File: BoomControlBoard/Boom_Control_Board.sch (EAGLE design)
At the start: 31 parts, among them IC1 L298, J1 Servo Header, J2 FTDI Header, U1 ATMEGA328P_TQFP, Y1 16MHz

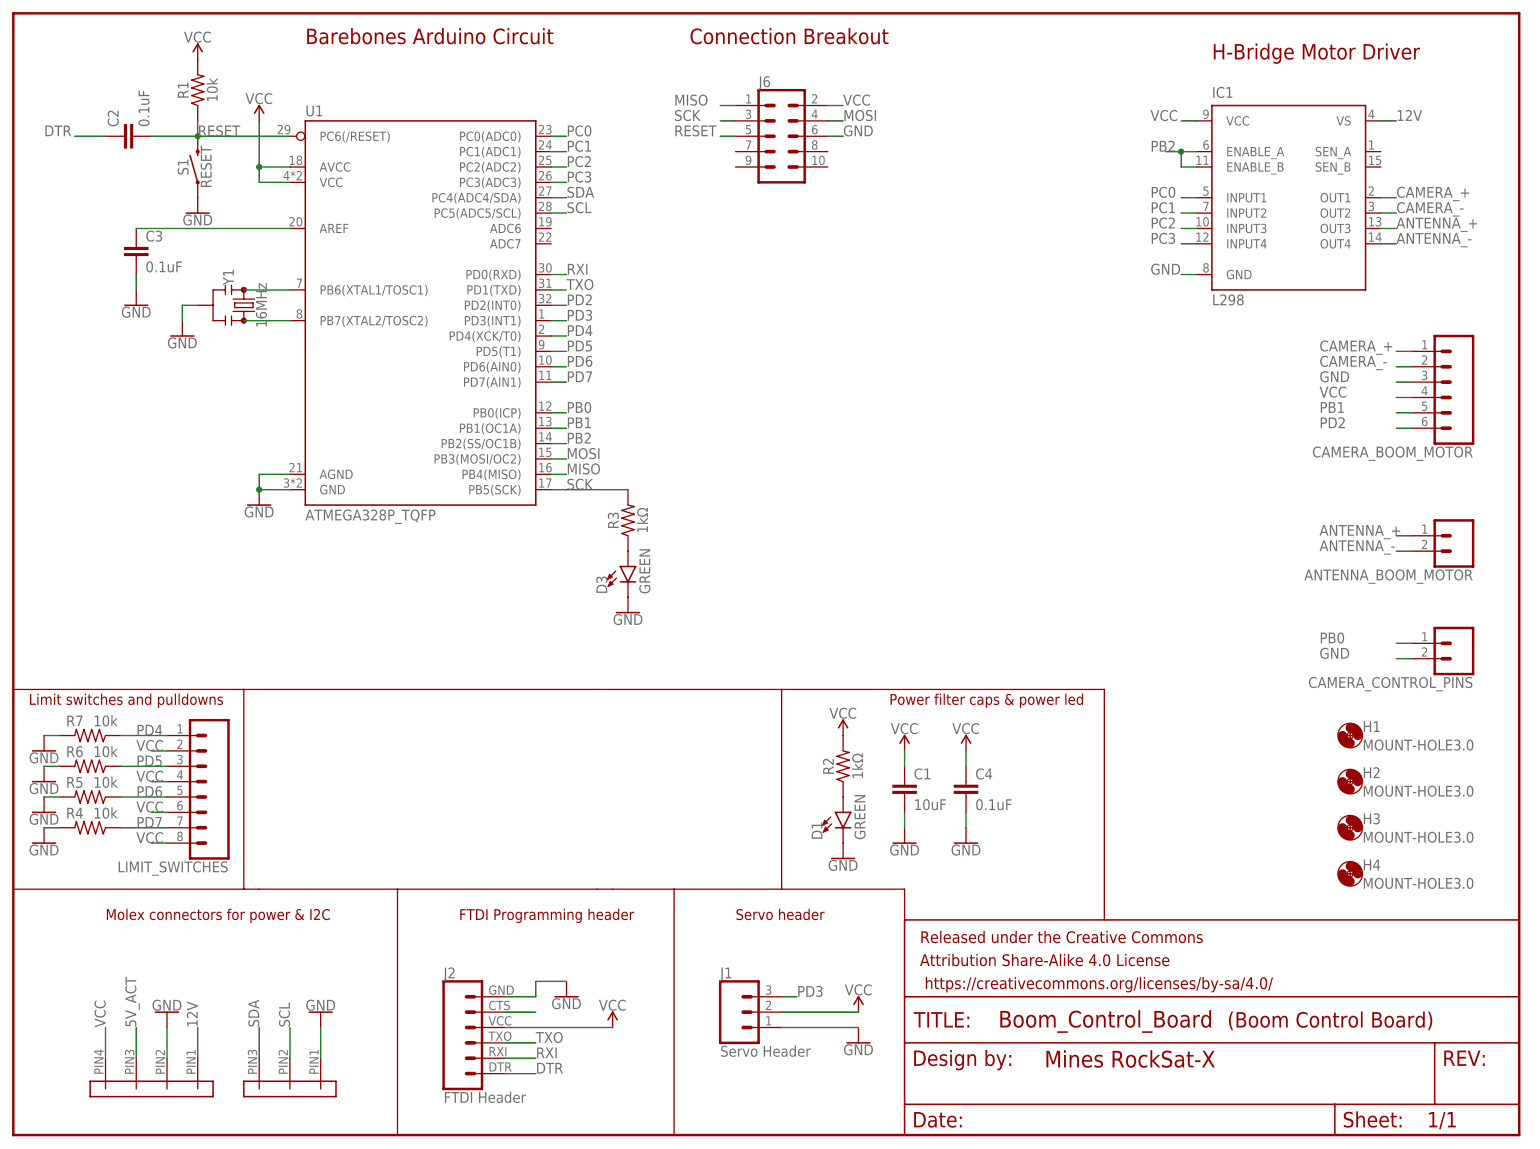
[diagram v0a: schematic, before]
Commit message: minor aesthetic adjustments to boom control board schem
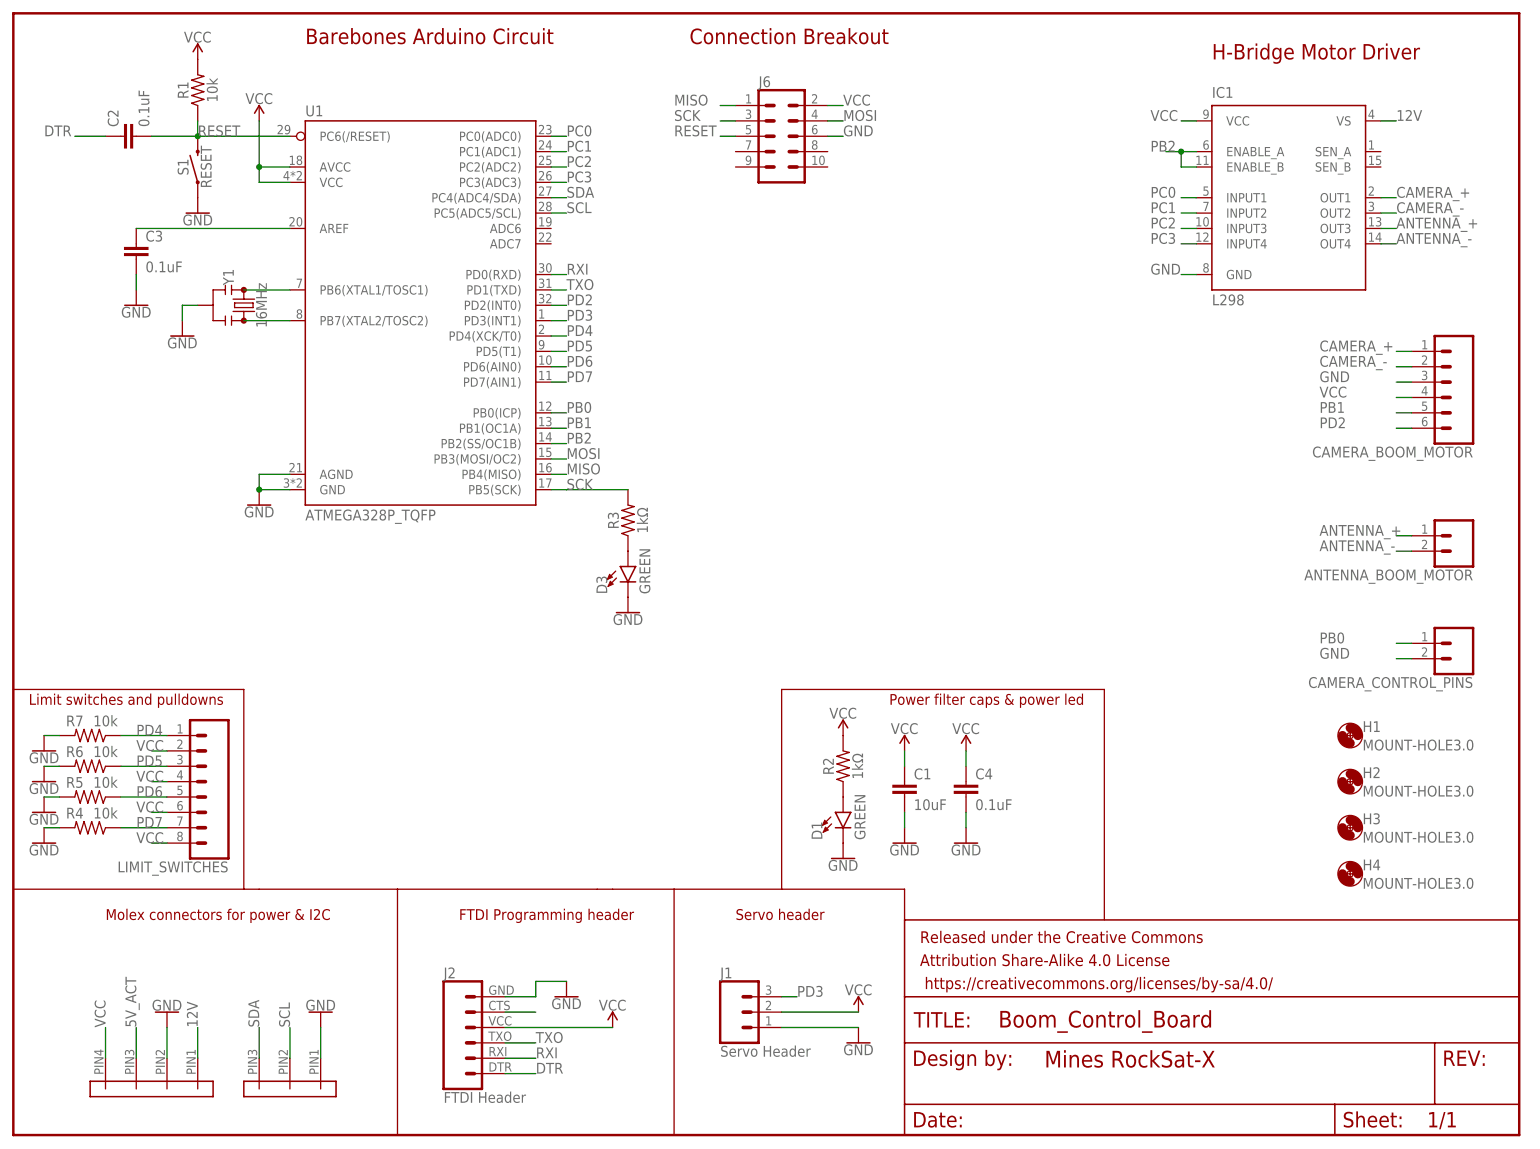
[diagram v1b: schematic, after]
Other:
- note removed: "(Boom Control Board)"

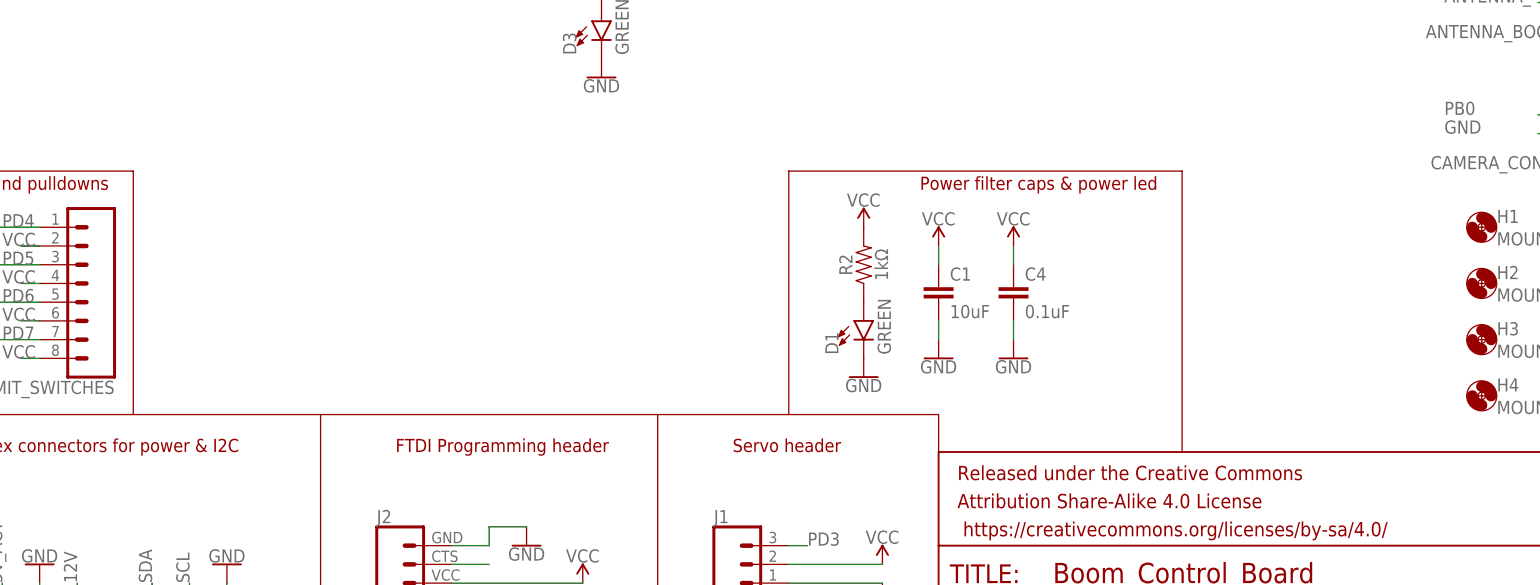
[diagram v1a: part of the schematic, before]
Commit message: Added RF module to Boom Control Board.
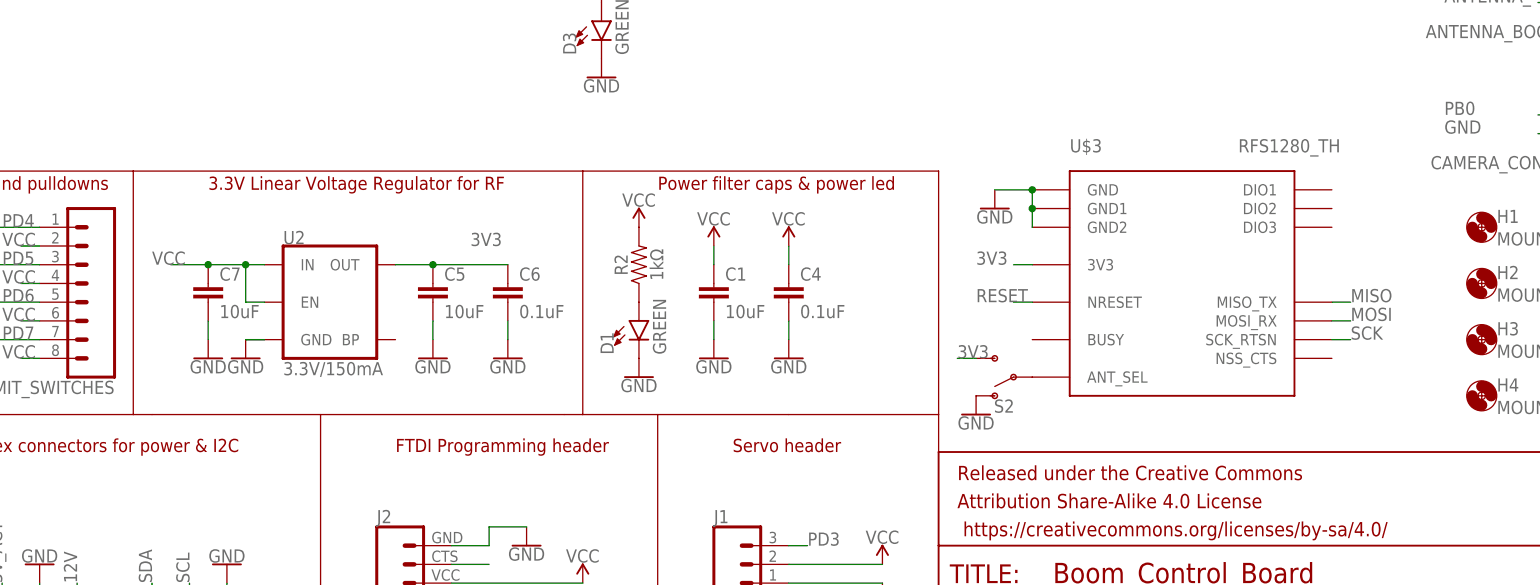
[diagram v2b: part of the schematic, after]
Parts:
- added C5, C7: 10uF, SparkFun-Capacitors:10UF-0805-10V-10%
- added C6: 0.1uF, SparkFun-Capacitors:2.2UF-0805-25V-(+80/-20%)
- added S2: (no value), SparkFun-Switches:SWITCH-SPDT-PTH-11.6X4.0MM
- added U$3: RFS1280_TH, PowerManagementParts:RFS1280_TH
- added U2: 3.3V/150mA, SparkFun-IC-Power:V_REG_MIC52053.3V
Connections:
- new net 3V3: C5.1, C6.1, S2.S, U$3.3V3, U2.OUT
- new net N$1: S2.P, U$3.ANT_SEL
- net GND: now also C5.2, C6.2, C7.2, S2.O, U$3.GND, U$3.GND1, U$3.GND2, U2.GND
- net MISO: now also U$3.MISO_TX
- net MOSI: now also U$3.MOSI_RX
- net RESET: now also U$3.NRESET
- net SCK: now also U$3.SCK_RTSN
- net VCC: now also C7.1, U2.EN, U2.IN
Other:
- note added: "3.3V Linear Voltage Regulator for RF"
- moved on the sheet: C1, C4, D1, R2

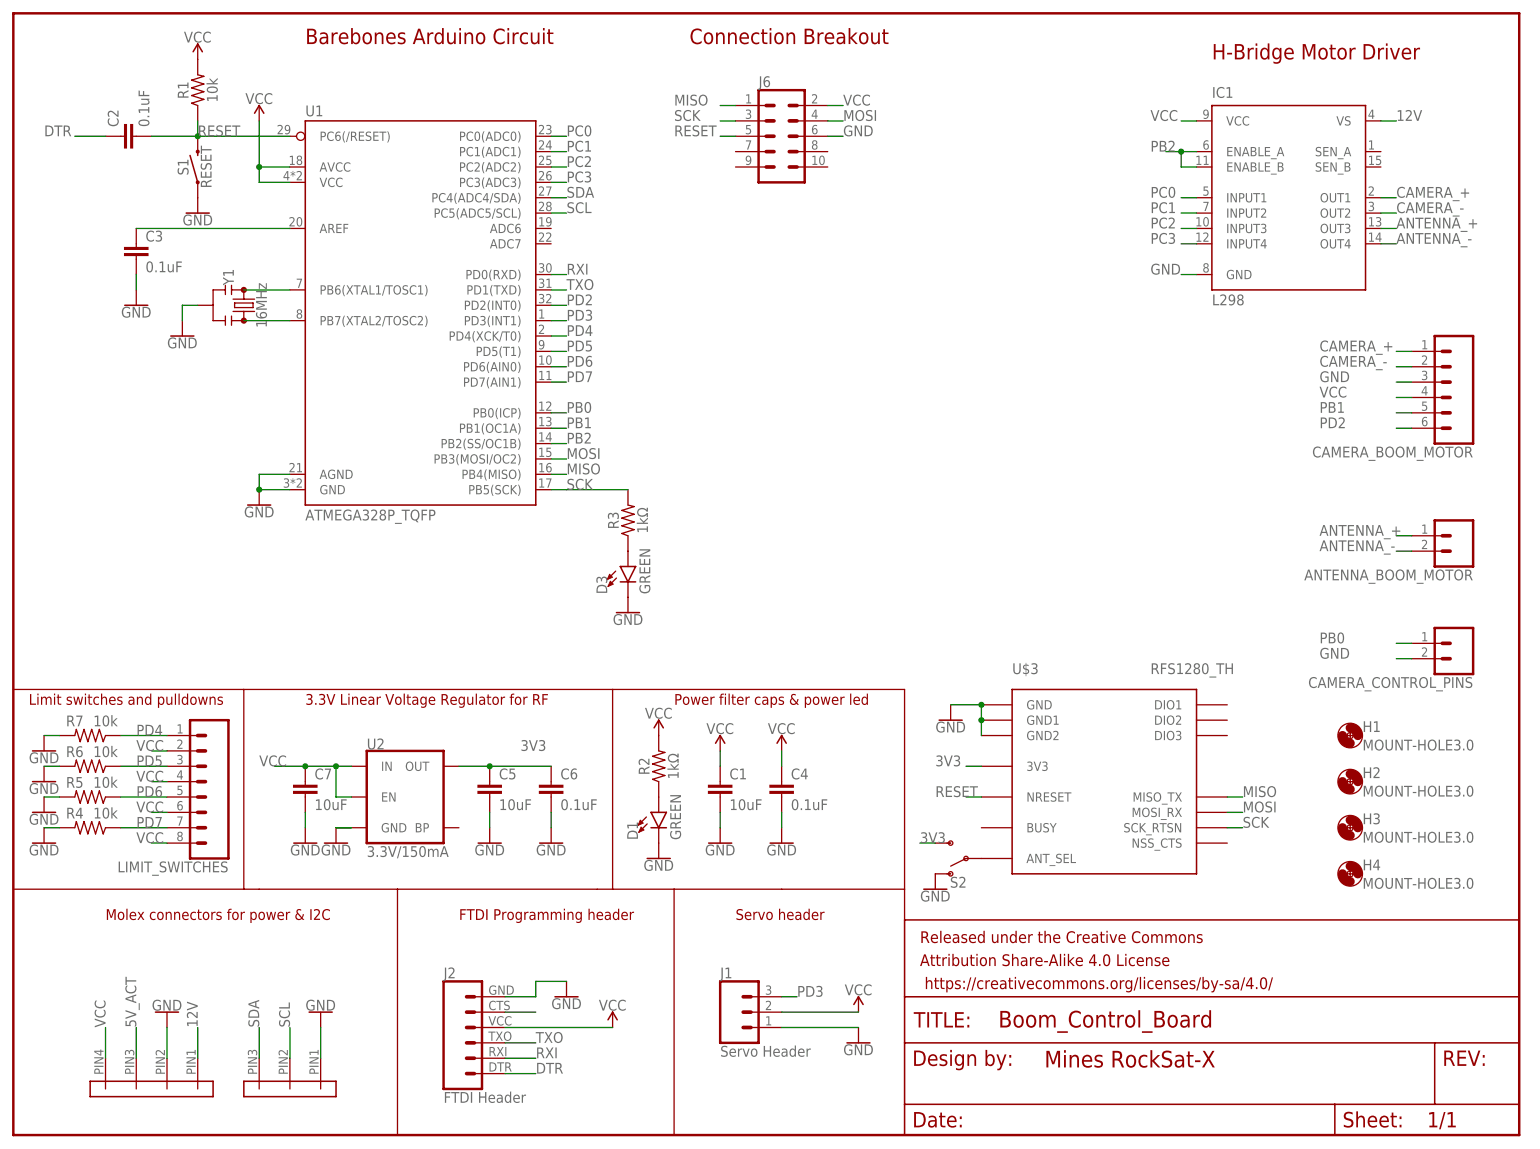
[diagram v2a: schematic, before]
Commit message: Finished routing Boom Control Board, added breakout points and labels. Swapped L298 for SMD part and swapped to dual SMD/TH RF Module footprint.
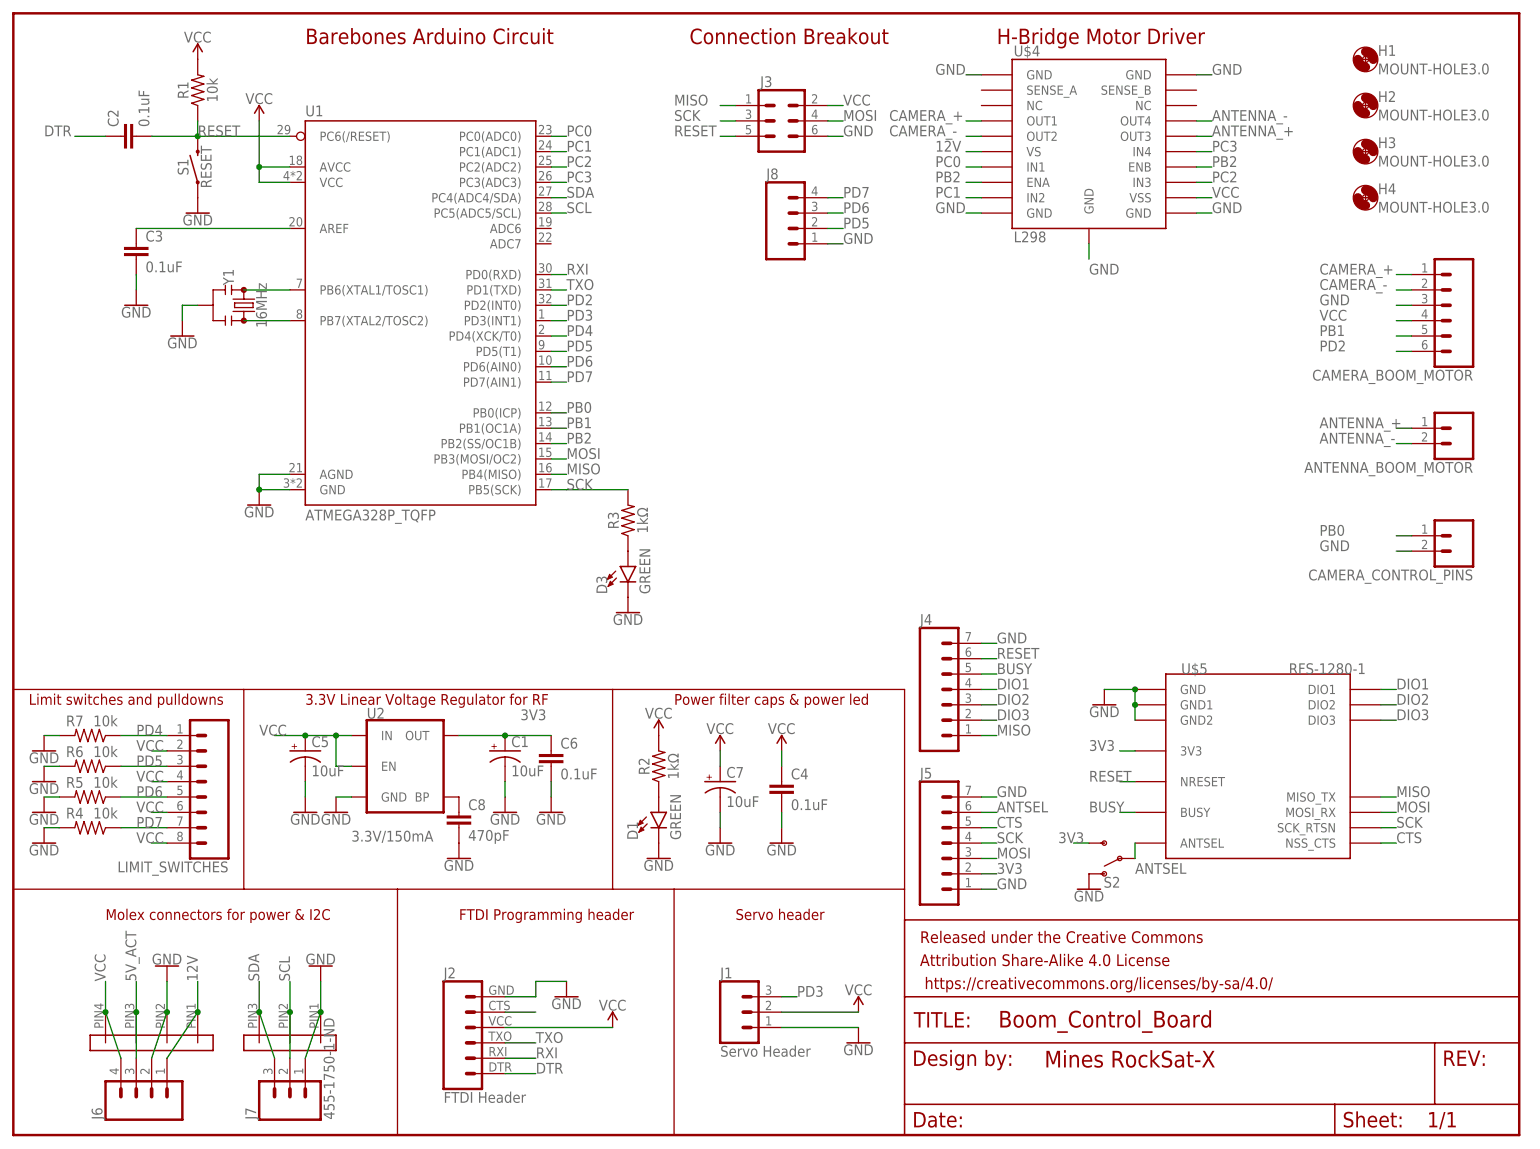
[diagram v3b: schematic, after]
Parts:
- removed IC1: L298, st-microelectronics:L298
- removed U$3: RFS1280_TH, PowerManagementParts:RFS1280_TH
- added C8: 470pF, SparkFun-Capacitors:CAP-0805
- added J3: (no value), SparkFun-Connectors:CONN_03X22X3_SILK_MALE_PTH
- added J4, J5: (no value), SparkFun-Connectors:CONN_07LOCK
- added J7: 455-1750-1-ND, SparkFun-Connectors:CONN_03
- added J8: (no value), SparkFun-Connectors:CONN_04LOCK
- added U$4: L298, SparkFun-IC-Special-Function:L298_SMD_W_PAD
- added U$5: RFS-1280-1, PowerManagementParts:RFS-1280-1
- C1, C5, C7: device SparkFun-Capacitors:10UF-0805-10V-10% -> SparkFun-Capacitors:10UF-POLAR-EIA3216-16V-10%(TANT)
- J6: device SparkFun-Connectors:CONN_05X2PTH -> SparkFun-Connectors:CONN_04LOCK
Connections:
- removed net N$1: S2.P, U$3.ANT_SEL
- new net ANTSEL: J5.6, S2.P, U$5.ANTSEL
- new net BUSY: J4.5, U$5.BUSY
- new net CTS: J5.5, U$5.NSS_CTS
- new net DIO1: J4.4, U$5.DIO1
- new net DIO2: J4.3, U$5.DIO2
- new net DIO3: J4.2, U$5.DIO3
- new net N$8: C8.1, U2.BP
- net 12V: now also J6.1, U$4.VS; no longer IC1.VS
- net 3V3: now also C1.+, J5.2, U$5.3V3; no longer C5.1, U$3.3V3
- net 5V_ACT: now also J6.3
- net ANTENNA_+: now also U$4.OUT3; no longer IC1.OUT3
- net ANTENNA_-: now also U$4.OUT4; no longer IC1.OUT4
- net CAMERA_+: now also U$4.OUT1; no longer IC1.OUT1
- net CAMERA_-: now also U$4.OUT2; no longer IC1.OUT2
- net GND: now also C1.-, C5.-, C7.-, C8.2, J3.6, J4.7, J5.1, J5.7, J6.2, J7.1, J8.1, U$4.GND@1, U$4.GND@10, U$4.GND@11, U$4.GND@20, U$4.GND@PAD, U$5.GND, U$5.GND1, U$5.GND2; no longer C1.2, C5.2, C7.2, IC1.GND, J6.6, U$3.GND, U$3.GND1, U$3.GND2
- net MISO: now also J3.1, J4.1, U$5.MISO_TX; no longer J6.1, U$3.MISO_TX
- net MOSI: now also J3.4, J5.3, U$5.MOSI_RX; no longer J6.4, U$3.MOSI_RX
- net PB2: now also U$4.ENA, U$4.ENB; no longer IC1.ENABLE_A, IC1.ENABLE_B
- net PC0: now also U$4.IN1; no longer IC1.INPUT1
- net PC1: now also U$4.IN2; no longer IC1.INPUT2
- net PC2: now also U$4.IN3; no longer IC1.INPUT3
- net PC3: now also U$4.IN4; no longer IC1.INPUT4
- net PD5: now also J8.2
- net PD6: now also J8.3
- net PD7: now also J8.4
- net RESET: now also J3.5, J4.6, U$5.NRESET; no longer J6.5, U$3.NRESET
- net SCK: now also J3.3, J5.4, U$5.SCK_RTSN; no longer J6.3, U$3.SCK_RTSN
- net SCL: now also J7.2
- net SDA: now also J7.3
- net VCC: now also C5.+, C7.+, J3.2, J6.4, U$4.VSS; no longer C1.1, C7.1, IC1.VCC, J6.2
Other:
- moved on the sheet: ANTENNA_BOOM_MOTOR, C6, CAMERA_BOOM_MOTOR, CAMERA_CONTROL_PINS, H1, H2, H3, H4, S2, U2
